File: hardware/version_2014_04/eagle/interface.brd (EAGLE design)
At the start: 63.9 x 21.7 mm, 19 parts

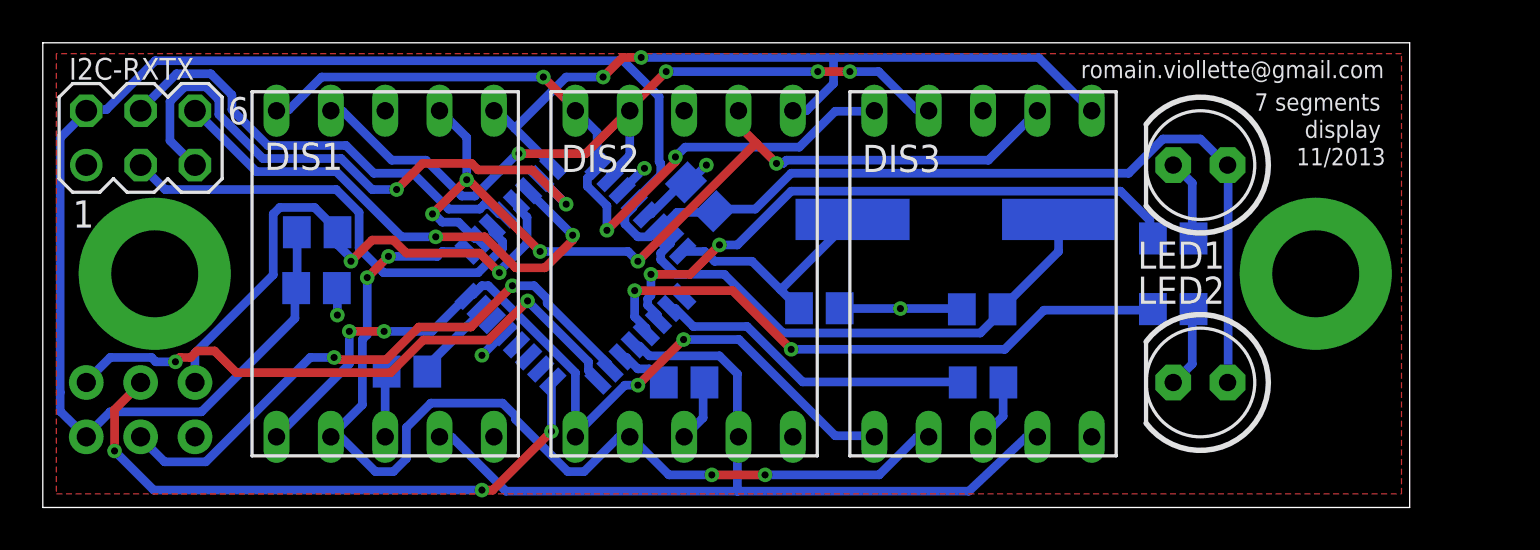
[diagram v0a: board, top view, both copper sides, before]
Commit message: mirrored RXTX connector
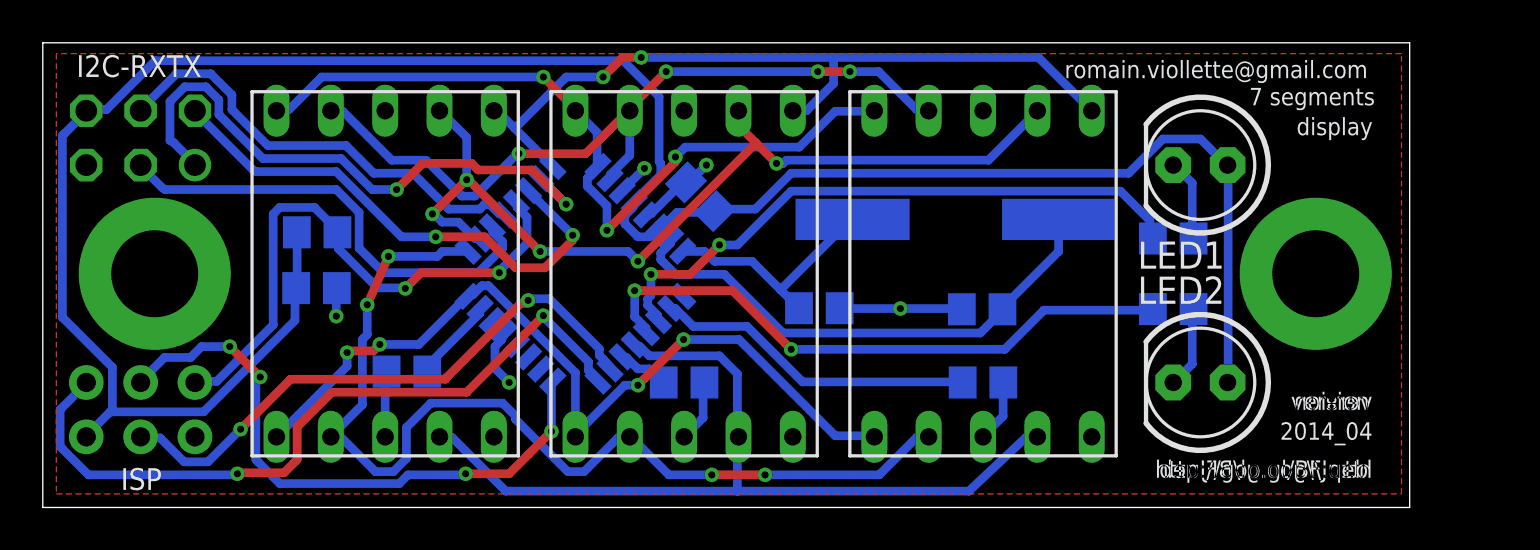
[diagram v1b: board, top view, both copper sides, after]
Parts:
- flipped I2C-RXTX to the bottom
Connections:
- net +5V: now also I2C-RXTX.6; no longer I2C-RXTX.2
- net GND: now also I2C-RXTX.5; no longer I2C-RXTX.1
- net RX: now also I2C-RXTX.2; no longer I2C-RXTX.6
- net TX: now also I2C-RXTX.1; no longer I2C-RXTX.5
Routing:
- net MISO: track 28.3 -> 34.9 mm
- net GND: track 13.7 -> 15.2 mm
- net SCK: track 28.4 -> 28.8 mm, vias 3 -> 4
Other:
- board text added: "2014_04"
- board text added: "RST"
- board text added: "http://goo.gl/BFJueb"
- board text added: "version"
- board text removed: "11/2013"
- board text removed: "RESET"
